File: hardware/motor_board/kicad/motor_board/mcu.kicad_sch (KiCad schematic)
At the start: 58 parts, among them J1 BOOMELE_1.27-2x10P, U1 STM32G474RET6, U5 AP2112K-3.3TRG1

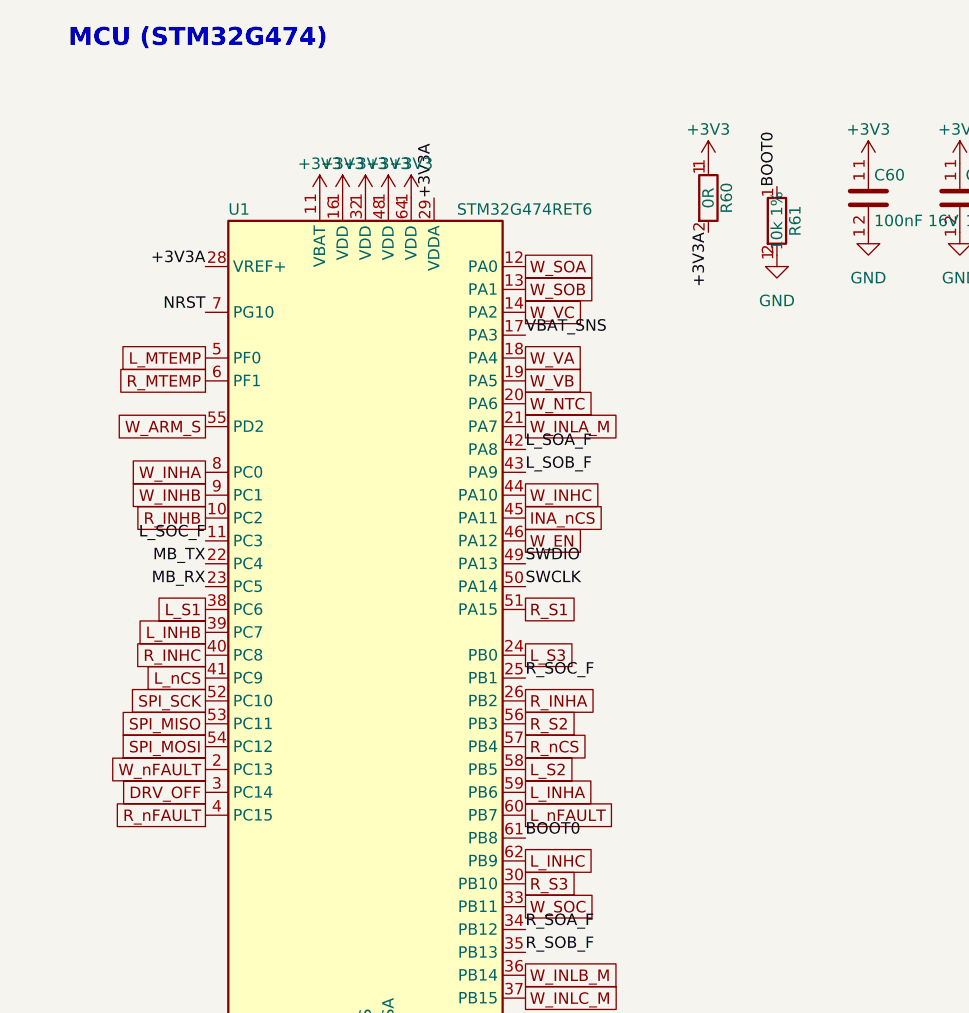
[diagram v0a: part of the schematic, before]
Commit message: MCU pin swaps for routing (rev L1): L_S2 -> PB4, L_S1 -> PB5, R_nCS -> PA11, INA_nCS -> PB8-BOOT0 (R61 removed, nSWBOOT0/nBOOT0 option bytes), PC6 unused; netlist/pinmap/schematic/DESIGN updated; tail swap_pin / del_fp ops; DRC 0, parity 0, 35 open
Co-Authored-By: Claude Opus 5.5 (1M context) <noreply@anthropic.com>
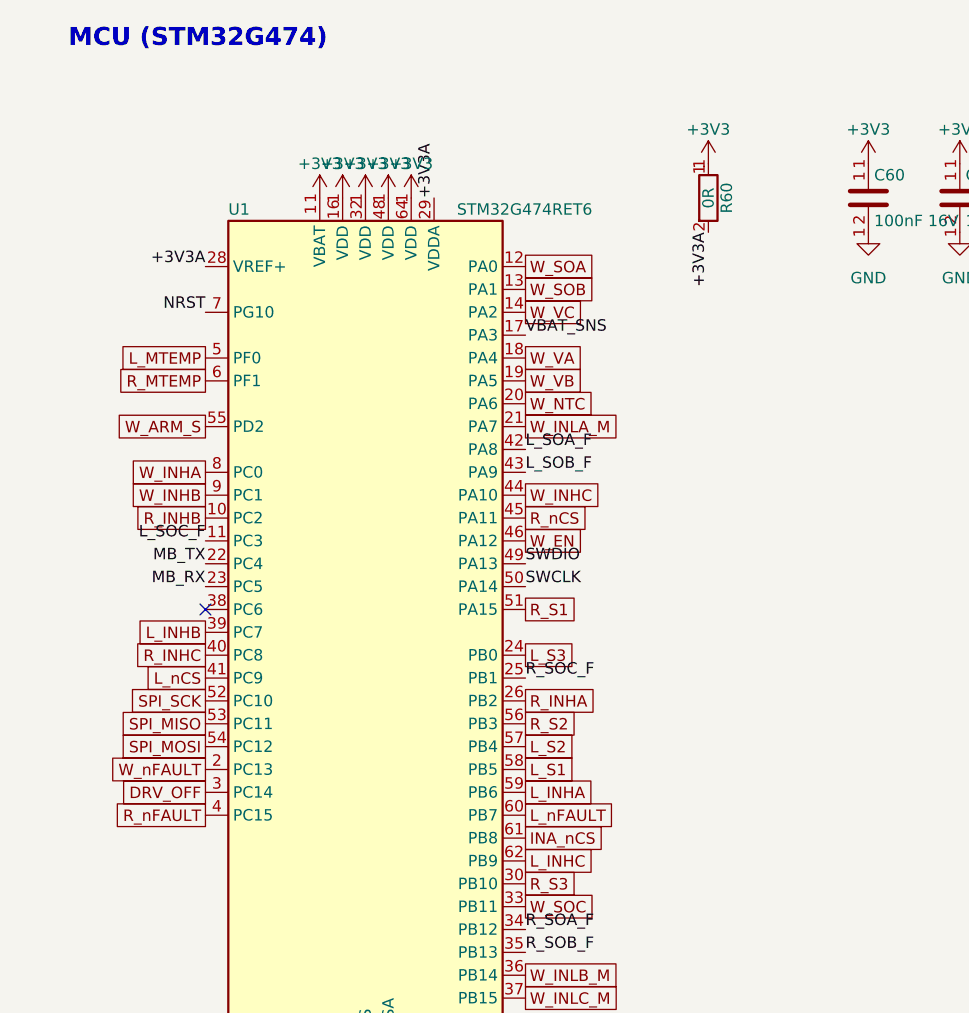
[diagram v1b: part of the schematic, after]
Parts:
- removed R61: 10k 1%, Resistor_SMD:R_0402_1005Metric, symbol Device:R
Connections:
- net BOOT0 is gone; now on net INA_nCS: U1.61 (PB8)
- net INA_nCS: no longer U1.45 (PA11)
- net L_S1: now also U1.58 (PB5); no longer U1.38 (PC6)
- net L_S2: now also U1.57 (PB4); no longer U1.58 (PB5)
- net R_nCS: now also U1.45 (PA11); no longer U1.57 (PB4)
- no-connect marks 3 -> 4
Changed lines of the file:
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@@
 		)
 	)
-	(global_label "L_S1"
-		(shape passive)
-		(at 40.64 88.9 180)
-		(fields_autoplaced yes)
-		(effects
-			(font
-				(size 1.27 1.27)
-			)
-			(justify right)
-		)
-		(property "Intersheetrefs" "${INTERSHEET_REFS}"
-			(at 40.64 88.9 0)
-			(effects
-				(font
-					(size 1.27 1.27)
-				)
-				(hide yes)
-			)
-		)
+	(no_connect
+		(at 40.64 88.9)
 	)
 	(global_label "L_INHB"
@@
 		)
 	)
-	(global_label "INA_nCS"
+	(global_label "R_nCS"
 		(shape passive)
 		(at 76.2 78.74 0)
@@
 		)
 	)
-	(global_label "R_nCS"
+	(global_label "L_S2"
 		(shape passive)
 		(at 76.2 104.14 0)
@@
 		)
 	)
-	(global_label "L_S2"
+	(global_label "L_S1"
 		(shape passive)
 		(at 76.2 106.68 0)
@@
 		)
 	)
-	(label "BOOT0"
+	(global_label "INA_nCS"
+		(shape passive)
 		(at 76.2 114.3 0)
 		(fields_autoplaced yes)
@@
 				(size 1.27 1.27)
 			)
-			(justify left bottom)
+			(justify left)
+		)
+		(property "Intersheetrefs" "${INTERSHEET_REFS}"
+			(at 76.2 114.3 0)
+			(effects
+				(font
+					(size 1.27 1.27)
+				)
+				(hide yes)
+			)
 		)
 	)
@@
 		)
 	)
-	(symbol
-		(lib_id "Device:R")
-		(at 104.14 45.72 0)
-		(unit 1)
-		(exclude_from_sim no)
-		(in_bom yes)
-		(on_board yes)
-		(dnp no)
-		(fields_autoplaced no)
-		(property "Reference" "R61"
-			(at 106.172 45.72 90)
-			(effects
-				(font
-					(size 1.27 1.27)
-				)
-			)
-		)
-		(property "Value" "10k 1%"
-			(at 104.14 45.72 90)
-			(effects
-				(font
-					(size 1.27 1.27)
-				)
-			)
-		)
-		(property "Footprint" "Resistor_SMD:R_0402_1005Metric"
-			(at 102.362 45.72 90)
-			(hide yes)
-			(effects
-				(font
-					(size 1.27 1.27)
-				)
-			)
-		)
-		(property "Datasheet" ""
-			(at 104.14 45.72 0)
-			(hide yes)
-			(effects
-				(font
-					(size 1.27 1.27)
-				)
-			)
-		)
-		(property "Description" "Resistor"
-			(at 104.14 45.72 0)
-			(hide yes)
-			(effects
-				(font
-					(size 1.27 1.27)
-				)
-			)
-		)
-		(property "LCSC" "C25744"
-			(at 104.14 45.72 0)
-			(hide yes)
-			(effects
-				(font
-					(size 1.27 1.27)
-				)
-			)
-		)
-		(pin "1"
-		)
-		(pin "2"
-		)
-		(instances
-			(project "motor_board"
-				(path "/171e0a5d-7eac-4b29-8fcf-e7df83310741/930effe6-f1bc-4e4e-aebc-c98263d4a033"
-					(reference "R61")
-					(unit 1)
-				)
-			)
-		)
-	)
-	(label "BOOT0"
-		(at 104.14 41.91 90)
-		(fields_autoplaced yes)
-		(effects
-			(font
-				(size 1.27 1.27)
-			)
-			(justify left bottom)
-		)
-	)
-	(symbol
-		(lib_id "power:GND")
-		(at 104.14 49.53 0)
-		(unit 1)
-		(exclude_from_sim no)
-		(in_bom no)
-		(on_board yes)
-		(dnp no)
-		(fields_autoplaced no)
-		(property "Reference" "#PWR0135"
-			(at 104.14 55.88 0)
-			(hide yes)
-			(effects
-				(font
-					(size 1.27 1.27)
-				)
-			)
-		)
-		(property "Value" "GND"
-			(at 104.14 54.61 0)
-			(effects
-				(font
-					(size 1.27 1.27)
-				)
-			)
-		)
-		(property "Footprint" ""
-			(at 104.14 49.53 0)
-			(hide yes)
-			(effects
-				(font
-					(size 1.27 1.27)
-				)
-			)
-		)
-		(property "Datasheet" ""
-			(at 104.14 49.53 0)
-			(hide yes)
-			(effects
-				(font
-					(size 1.27 1.27)
-				)
-			)
-		)
-		(property "Description" ""
-			(at 104.14 49.53 0)
-			(hide yes)
-			(effects
-				(font
-					(size 1.27 1.27)
-				)
-			)
-		)
-		(pin "1"
-		)
-		(instances
-			(project "motor_board"
-				(path "/171e0a5d-7eac-4b29-8fcf-e7df83310741/930effe6-f1bc-4e4e-aebc-c98263d4a033"
-					(reference "#PWR0135")
-					(unit 1)
-				)
-			)
-		)
-	)

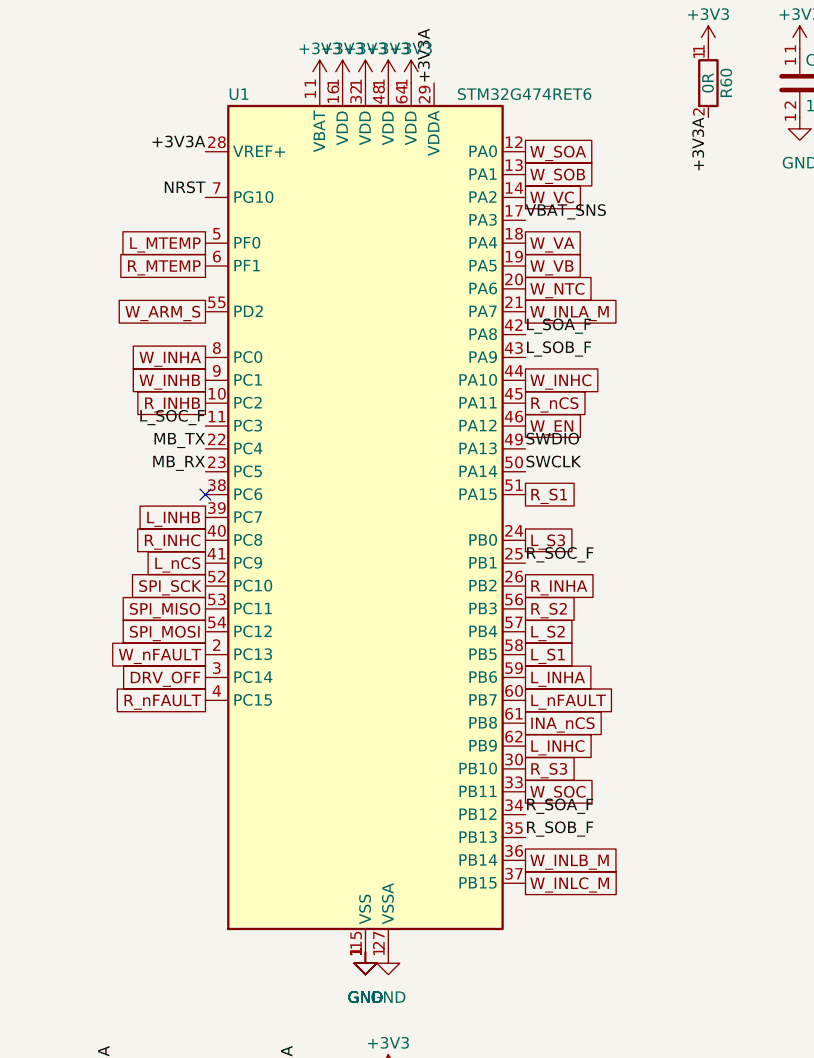
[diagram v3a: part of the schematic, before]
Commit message: Rev L3: MCU pin map co-assigned with the v2 placement (kicad/v2/pinsolve.py, CP-SAT on the real pads): architecture unchanged (TIM1 weapon, TIM8/TIM20 drives, TIM3/TIM2 sensors, ADC5 drive L, ADC3/4 drive R, SPI3, USART1); break inputs on BKIN only, one port per EXTI line, motor-NTC inputs on 5 V-tolerant pins, PB8-BOOT0 on a pulled-up chip select; DESIGN 3.x/7/8/9 and CHANGES updated (ADC ranks re-derived); schematic regenerated (176/176), board rebuilt and re-placed (U4 rotated, JR on the rear edge, J3 + sensor R front end at the rear-right); global router (groute.py, gate.py, gstats.py) with v1 calibration; Freerouting trial script
Co-Authored-By: Claude Opus 5.5 (1M context) <noreply@anthropic.com>
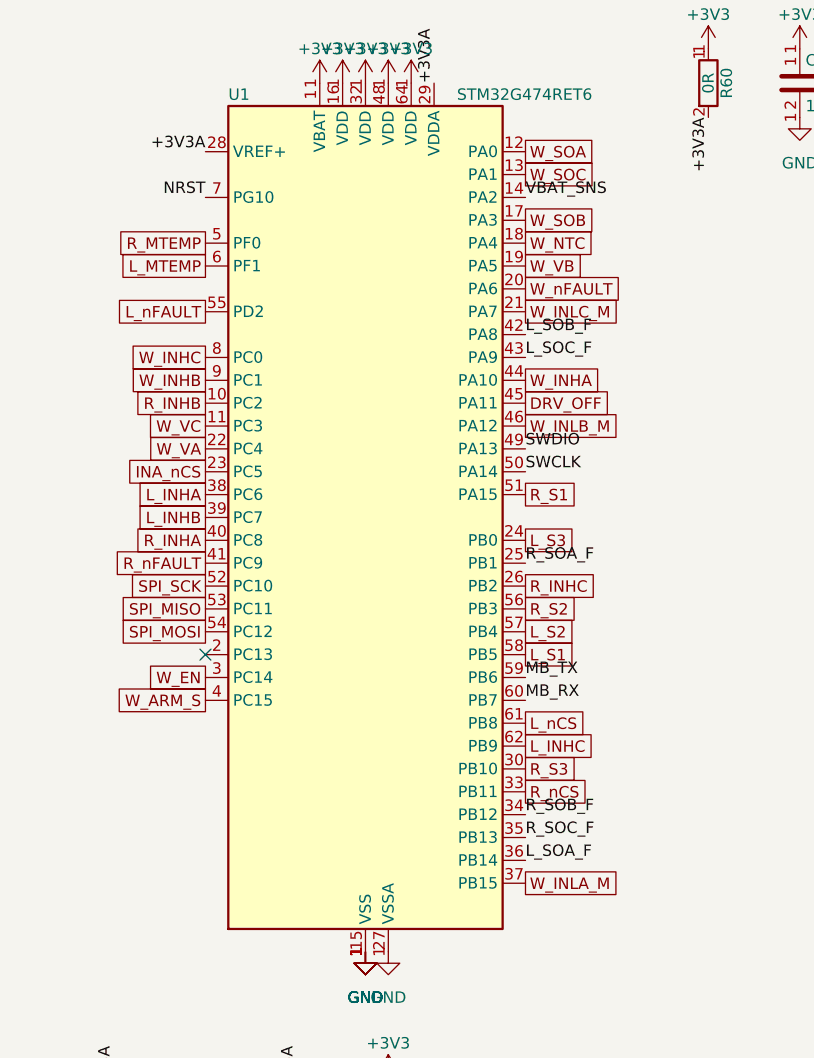
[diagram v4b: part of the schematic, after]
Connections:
- net DRV_OFF: now also U1.45 (PA11); no longer U1.3 (PC14)
- net INA_nCS: now also U1.23 (PC5); no longer U1.61 (PB8)
- net L_INHA: now also U1.38 (PC6); no longer U1.59 (PB6)
- net L_MTEMP: now also U1.6 (PF1); no longer U1.5 (PF0)
- net L_SOA_F: now also U1.36 (PB14); no longer U1.42 (PA8)
- net L_SOB_F: now also U1.42 (PA8); no longer U1.43 (PA9)
- net L_SOC_F: now also U1.43 (PA9); no longer U1.11 (PC3)
- net L_nCS: now also U1.61 (PB8); no longer U1.41 (PC9)
- net L_nFAULT: now also U1.55 (PD2); no longer U1.60 (PB7)
- net MB_RX: now also U1.60 (PB7); no longer U1.23 (PC5)
- net MB_TX: now also U1.59 (PB6); no longer U1.22 (PC4)
- net R_INHA: now also U1.40 (PC8); no longer U1.26 (PB2)
- net R_INHC: now also U1.26 (PB2); no longer U1.40 (PC8)
- net R_MTEMP: now also U1.5 (PF0); no longer U1.6 (PF1)
- net R_SOA_F: now also U1.25 (PB1); no longer U1.34 (PB12)
- net R_SOB_F: now also U1.34 (PB12); no longer U1.35 (PB13)
- net R_SOC_F: now also U1.35 (PB13); no longer U1.25 (PB1)
- net R_nCS: now also U1.33 (PB11); no longer U1.45 (PA11)
- net R_nFAULT: now also U1.41 (PC9); no longer U1.4 (PC15)
- net VBAT_SNS: now also U1.14 (PA2); no longer U1.17 (PA3)
- net W_ARM_S: now also U1.4 (PC15); no longer U1.55 (PD2)
- net W_EN: now also U1.3 (PC14); no longer U1.46 (PA12)
- net W_INHA: now also U1.44 (PA10); no longer U1.8 (PC0)
- net W_INHC: now also U1.8 (PC0); no longer U1.44 (PA10)
- net W_INLA_M: now also U1.37 (PB15); no longer U1.21 (PA7)
- net W_INLB_M: now also U1.46 (PA12); no longer U1.36 (PB14)
- net W_INLC_M: now also U1.21 (PA7); no longer U1.37 (PB15)
- net W_NTC: now also U1.18 (PA4); no longer U1.20 (PA6)
- net W_SOB: now also U1.17 (PA3); no longer U1.13 (PA1)
- net W_SOC: now also U1.13 (PA1); no longer U1.33 (PB11)
- net W_VA: now also U1.22 (PC4); no longer U1.18 (PA4)
- net W_VC: now also U1.11 (PC3); no longer U1.14 (PA2)
- net W_nFAULT: now also U1.20 (PA6); no longer U1.2 (PC13)

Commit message: Schematic regenerated for C117 + U7 INA239AQDGSRQ1 (lib_build parts/symbol, SHEETS/blocks); board sync stage hR (tail_apply op 'sync' via schsync.py: footprints re-linked to the new symbol UUIDs, U7 fields, C117 added provisionally near U8 and routed); r2/pourtest.py power-net pour acceptance test (12 nets failing on hF: the rework list); DRC 0, parity 0
Co-Authored-By: Claude Opus 5.5 (1M context) <noreply@anthropic.com>
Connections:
- net BMS_ALERT: now also J1.5 (Pin_5); no longer J1.17 (Pin_17)
- net BMS_SCL: now also J1.6 (Pin_6); no longer J1.16 (Pin_16)
- net BMS_SDA: now also J1.3 (Pin_3); no longer J1.15 (Pin_15)
- net GND: now also J1.11 (Pin_11), J1.15 (Pin_15); no longer J1.12 (Pin_12), J1.3 (Pin_3)
- net L_S1: now also U1.51 (PA15); no longer U1.58 (PB5)
- net L_S2: now also U1.56 (PB3); no longer U1.57 (PB4)
- net L_S3: now also U1.30 (PB10); no longer U1.24 (PB0)
- net MB_RX: now also J1.19 (Pin_19); no longer J1.6 (Pin_6)
- net MB_TX: now also J1.17 (Pin_17); no longer J1.5 (Pin_5)
- net R_S1: now also U1.57 (PB4); no longer U1.51 (PA15)
- net R_S2: now also U1.58 (PB5); no longer U1.56 (PB3)
- net R_S3: now also U1.24 (PB0); no longer U1.30 (PB10)
- net VBAT_SNS_H: now also J1.12 (Pin_12); no longer J1.11 (Pin_11)
- net W_ARM_CLK: now also J1.18 (Pin_18); no longer J1.19 (Pin_19)
